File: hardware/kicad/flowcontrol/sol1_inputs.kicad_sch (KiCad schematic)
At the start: 3 parts, among them SW3 SOL1_DURA, SW4 SOL1_DELAY, SW9 SOL1_MASTER

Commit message: Schemiatic update
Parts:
- SW3, SW4: footprint (none) -> Rotary_Encoder:RotaryEncoder_Alps_EC11E_Vertical_H20mm
- SW9: footprint (none) -> Button_Switch_THT:SW_DIP_SPSTx01_Slide_6.7x4.1mm_W7.62mm_P2.54mm_LowProfile
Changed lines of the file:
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@@
 			)
 		)
-		(property "Footprint" ""
+		(property "Footprint" "Rotary_Encoder:RotaryEncoder_Alps_EC11E_Vertical_H20mm"
 			(at 83.82 25.146 0)
 			(effects
@@
 			)
 		)
-		(property "Footprint" ""
+		(property "Footprint" "Rotary_Encoder:RotaryEncoder_Alps_EC11E_Vertical_H20mm"
 			(at 52.07 25.146 0)
 			(effects
@@
 			)
 		)
-		(property "Footprint" ""
+		(property "Footprint" "Button_Switch_THT:SW_DIP_SPSTx01_Slide_6.7x4.1mm_W7.62mm_P2.54mm_LowProfile"
 			(at 55.88 58.42 0)
 			(effects

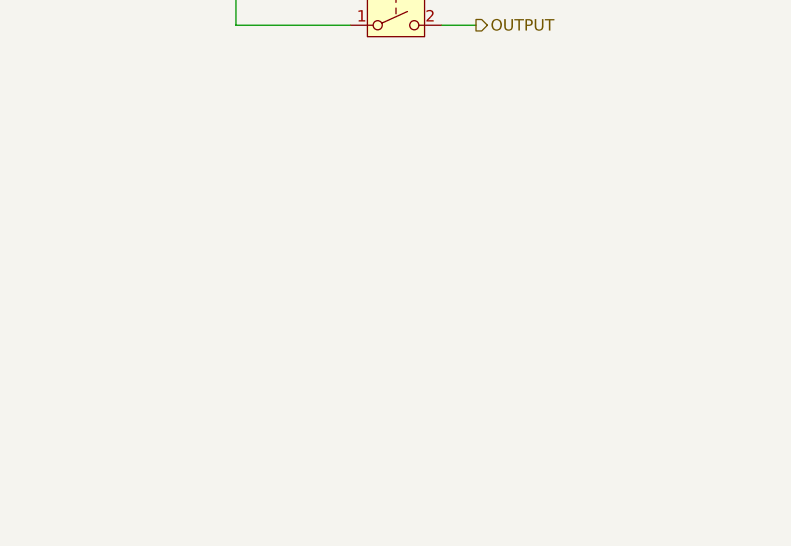
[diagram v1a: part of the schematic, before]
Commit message: Added Arduino coding
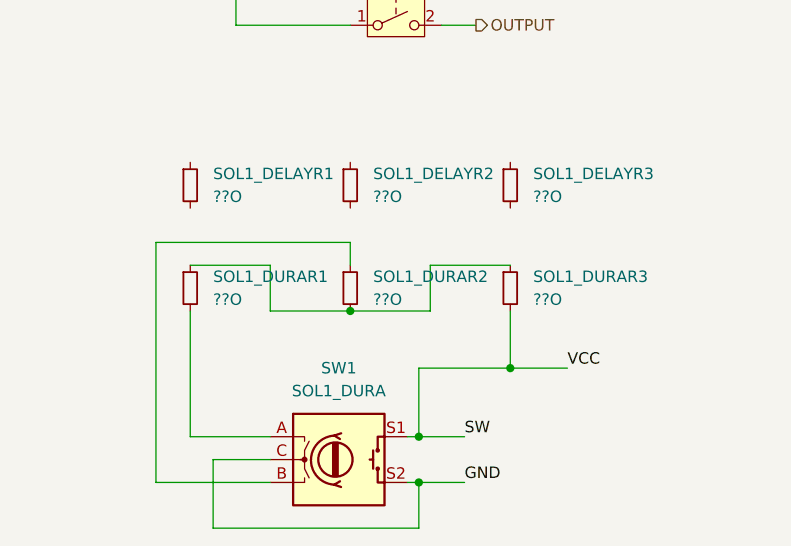
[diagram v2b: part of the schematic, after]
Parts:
- added SOL1_DELAYR1, SOL1_DELAYR2, SOL1_DELAYR3, SOL1_DURAR1, SOL1_DURAR2, SOL1_DURAR3: ??O, symbol Device:R_Small
- added SW1: SOL1_DURA, Rotary_Encoder:RotaryEncoder_Alps_EC11E_Vertical_H20mm, symbol Device:RotaryEncoder_Switch
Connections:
- net GND: now also SW1.C, SW1.S2
- net VCC: now also SOL1_DURAR3.2, SW1.S1
- new net: SOL1_DURAR2.1, SW1.B
- new net: SOL1_DURAR1.1, SOL1_DURAR2.2, SOL1_DURAR3.1
- new net: SOL1_DURAR1.2, SW1.A

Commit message: Updated KiCad schematic to final rendition
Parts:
- removed SOL1_DELAYR1, SOL1_DELAYR2, SOL1_DELAYR3, SOL1_DURAR1, SOL1_DURAR2, SOL1_DURAR3: ??O, symbol Device:R_Small
- removed SW1: SOL1_DURA, Rotary_Encoder:RotaryEncoder_Alps_EC11E_Vertical_H20mm, symbol Device:RotaryEncoder_Switch
- removed SW4: SOL1_DELAY, Rotary_Encoder:RotaryEncoder_Alps_EC11E_Vertical_H20mm, symbol Device:RotaryEncoder_Switch
- removed SW9: SOL1_MASTER, Button_Switch_THT:SW_DIP_SPSTx01_Slide_6.7x4.1mm_W7.62mm_P2.54mm_LowProfile, symbol Switch:SW_DPST
- added J1: 4-digit I2C Display, symbol Connector_Generic:Conn_01x04
- added U1: 5V Regulator, symbol Regulator_Linear:uA7805
- SW3: value SOL1_DURA -> DIAL
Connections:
- net CONFIRM renamed SWITCH
- net DURATION renamed DT
- net GND renamed GND_E
- net VCC renamed VCC_E
- new net 12V_R: U1.1 (IN)
- new net GND_R: U1.2 (GND)
- new net GND_S: J1.3 (Pin_3)
- new net SCL: J1.1 (Pin_1)
- new net SDA: J1.2 (Pin_2)
- new net VCC_R: U1.3 (OUT)
- new net VCC_S: J1.4 (Pin_4)
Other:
- added sheet Solenoid 2 Output1 (sol1_output.kicad_sch)

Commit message: labeled the old pcb old
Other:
- removed sheet Solenoid 2 Output1
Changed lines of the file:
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@@
 	)
 	(hierarchical_label "VCC_R"
-		(shape output)
+		(shape input)
 		(at 26.67 77.47 180)
 		(fields_autoplaced yes)
@@
 			)
 		)
-	)
-	(sheet
-		(at 170.18 115.57)
-		(size 17.78 22.86)
-		(fields_autoplaced yes)
-		(stroke
-			(width 0.1524)
-			(type solid)
-		)
-		(fill
-			(color 0 0 0 0.0000)
-		)
-		(property "Sheetname" "Solenoid 2 Output1"
-			(at 170.18 114.8584 0)
-			(effects
-				(font
-					(size 1.27 1.27)
-				)
-				(justify left bottom)
-			)
-		)
-		(property "Sheetfile" "sol1_output.kicad_sch"
-			(at 170.18 139.0146 0)
-			(effects
-				(font
-					(size 1.27 1.27)
-				)
-				(justify left top)
-			)
-		)
-		(pin "SETTING" input
-			(at 170.18 118.11 180)
-			(effects
-				(font
-					(size 1.27 1.27)
-				)
-				(justify left)
-			)
-		)
-		(pin "MAIN" input
-			(at 170.18 123.19 180)
-			(effects
-				(font
-					(size 1.27 1.27)
-				)
-				(justify left)
-			)
-		)
-		(pin "RED" input
-			(at 170.18 125.73 180)
-			(effects
-				(font
-					(size 1.27 1.27)
-				)
-				(justify left)
-			)
-		)
-		(pin "5V" input
-			(at 170.18 128.27 180)
-			(effects
-				(font
-					(size 1.27 1.27)
-				)
-				(justify left)
-			)
-		)
-		(pin "TRIGGER" input
-			(at 170.18 120.65 180)
-			(effects
-				(font
-					(size 1.27 1.27)
-				)
-				(justify left)
-			)
-		)
-		(pin "12V_SUPPLY" input
-			(at 182.88 138.43 270)
-			(effects
-				(font
-					(size 1.27 1.27)
-				)
-				(justify left)
-			)
-		)
-		(pin "GND_SUPPLY" input
-			(at 185.42 138.43 270)
-			(effects
-				(font
-					(size 1.27 1.27)
-				)
-				(justify left)
-			)
-		)
-		(pin "GND" input
-			(at 170.18 130.81 180)
-			(effects
-				(font
-					(size 1.27 1.27)
-				)
-				(justify left)
-			)
-		)

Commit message: semi-final updates for the report
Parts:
- J1: footprint (none) -> Connector_PinHeader_2.54mm:PinHeader_1x04_P2.54mm_Vertical
- SW3: footprint Rotary_Encoder:RotaryEncoder_Alps_EC11E_Vertical_H20mm -> Button_Switch_THT:RotaryEncoder_Vertical_H20mm
- U1: footprint (none) -> Package_TO_SOT_THT:TO-218-3_Vertical
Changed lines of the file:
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@@
 	)
 	(hierarchical_label "12V_R"
-		(shape input)
+		(shape output)
 		(at 26.67 72.39 180)
 		(fields_autoplaced yes)
@@
 	)
 	(hierarchical_label "GND_R"
-		(shape input)
+		(shape passive)
 		(at 26.67 74.93 180)
 		(fields_autoplaced yes)
@@
 			)
 		)
-		(property "Footprint" "Rotary_Encoder:RotaryEncoder_Alps_EC11E_Vertical_H20mm"
+		(property "Footprint" "Button_Switch_THT:RotaryEncoder_Vertical_H20mm"
 			(at 52.07 25.146 0)
 			(effects
@@
 			)
 		)
-		(property "Footprint" ""
+		(property "Footprint" "Package_TO_SOT_THT:TO-218-3_Vertical"
 			(at 56.515 76.2 0)
 			(effects
@@
 			)
 		)
-		(property "Footprint" ""
+		(property "Footprint" "Connector_PinHeader_2.54mm:PinHeader_1x04_P2.54mm_Vertical"
 			(at 55.88 54.61 0)
 			(effects
